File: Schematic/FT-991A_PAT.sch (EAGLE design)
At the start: 30 parts, among them Q1 PE4259, Q2 MC78L09ABDR2GOSCT, Q5 NCP553, Q7 J310, Q8 5086, X1 IF_IN, X2 SCP_OUT, X3 SDR_OUT

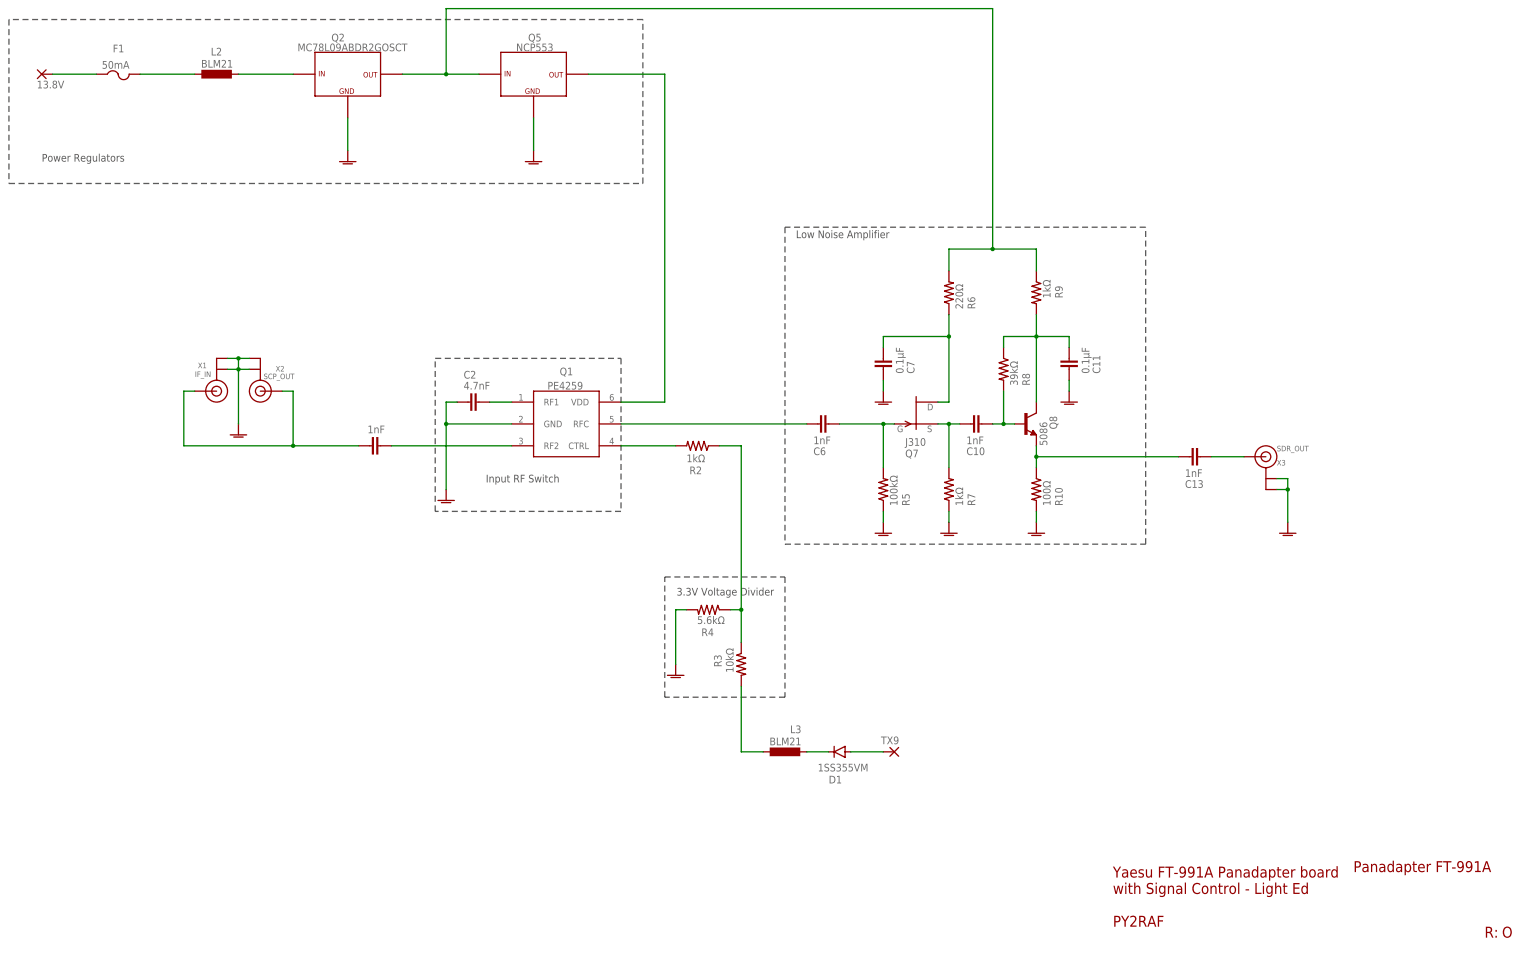
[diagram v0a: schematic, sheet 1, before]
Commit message: Starring: Revision P
* Repositioned the SDR Out port to right above the DC block cap
* Changed RF switch layout - now IF input uses the RF switch's `RFC`
  port instead of RF2 - It seems that the PE4259's `RF{N}` port gets in
  a grounded state instead of just reflecting out the data when not
  selected / active
* Got rid of the "Grounding" in RF1 port; that's not necessary
  because... Above
* Few text corrections
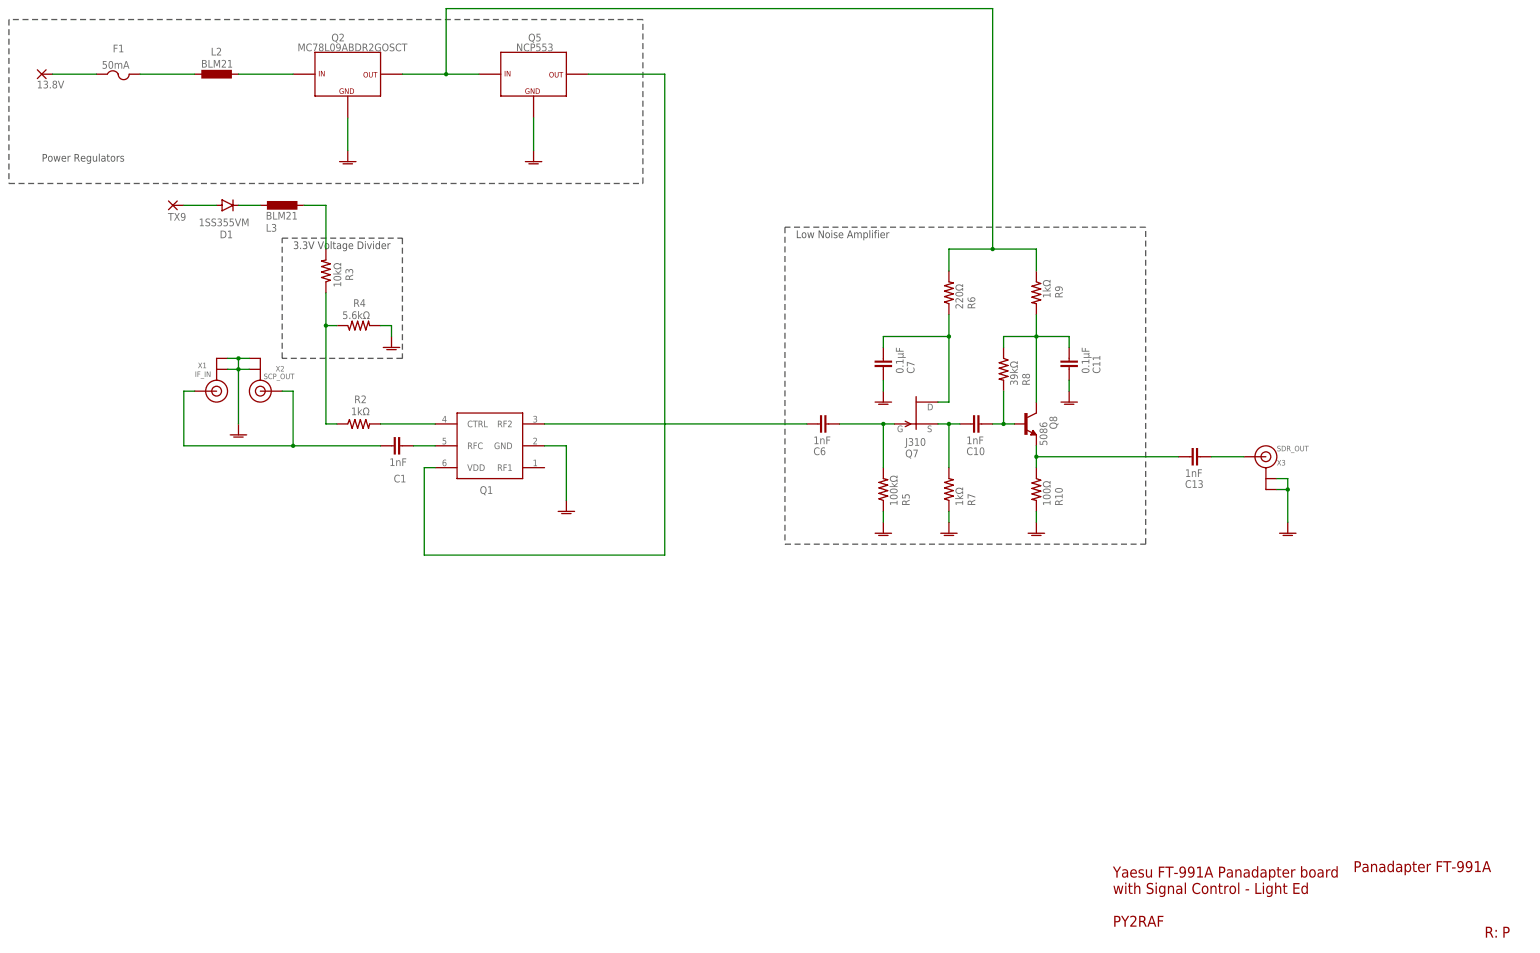
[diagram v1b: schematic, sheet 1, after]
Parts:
- removed C2: 4.7nF, rcl:C-EUC3216
- Q1: value PE4259 -> (none)
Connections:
- removed net N$21: C2.2, Q1.RF1
- removed net N$24: C1.2, Q1.RF2
- new net N$2: C1.2, Q1.RFC
- net GNDA: no longer C2.1
- net N$3: now also Q1.RF2; no longer Q1.RFC
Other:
- note removed: "DISABLE"
- note removed: "Input RF Switch"
- moved on the sheet: D1, L3, Q1, R2, R3, R4

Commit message: Board: Added test pads
Added test pads for 9V, 3V and RF Switch.
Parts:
- added TP1: 9V, testpad:TPB1,27
- added TP2, TP3: 3V, testpad:TPB1,27
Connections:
- net N$7: now also TP3.TP
- net VCC: now also TP1.TP
- net VDD: now also TP2.TP
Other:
- moved on the sheet: C1, C10, C11, C13, C6, C7, D1, F1, L2, L3, Q1, Q2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

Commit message: Preparing: Revision Q
* Better Silk-Screen Pin 1 markings for Power regulators
* Larger footprint for 2SC5086
* Moving 0.1µF transistor caps away from RF section
* Lots of re-routing
* Changing 1 nF caps to Low ESL type and 0805 footprint for better RF
  performance
* Labeled a few signals in Eagle file for better understanding of signal
  route/path
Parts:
- C1, C10, C13, C6: value 1nF -> 1000pF; device rcl:C-EUC3216 -> rcl:C-EUC0805
- Q1: value (none) -> PE4259
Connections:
- net N$10 renamed 9V5086
- net N$2 renamed IFTAP
- net N$3 renamed IFIN
- net N$37 renamed FINAL
- net N$9 renamed 9VJ310
- net VCC renamed 9V
- net VDD renamed 3V
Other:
- moved on the sheet: C13
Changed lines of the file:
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@@
 </classes>
 <parts>
-<part name="C6" library="rcl" library_urn="urn:adsk.eagle:library:334" deviceset="C-EU" device="C3216" package3d_urn="urn:adsk.eagle:package:23628/2" value="1nF"/>
+<part name="C6" library="rcl" library_urn="urn:adsk.eagle:library:334" deviceset="C-EU" device="C0805" package3d_urn="urn:adsk.eagle:package:23617/2" value="1000pF"/>
 <part name="R5" library="rcl" library_urn="urn:adsk.eagle:library:334" deviceset="R-US_" device="R3216" package3d_urn="urn:adsk.eagle:package:23557/2" value="100kΩ"/>
 <part name="Q7" library="transistor-fet" library_urn="urn:adsk.eagle:library:396" deviceset="?20*" device="SST" package3d_urn="urn:adsk.eagle:package:28534/2" technology="1" value="J310">
@@
 <part name="Q8" library="aarf" deviceset="2SC5086" device="" value="5086"/>
 <part name="R7" library="rcl" library_urn="urn:adsk.eagle:library:334" deviceset="R-US_" device="R3216" package3d_urn="urn:adsk.eagle:package:23557/2" value="1kΩ"/>
-<part name="C10" library="rcl" library_urn="urn:adsk.eagle:library:334" deviceset="C-EU" device="C3216" package3d_urn="urn:adsk.eagle:package:23628/2" value="1nF"/>
+<part name="C10" library="rcl" library_urn="urn:adsk.eagle:library:334" deviceset="C-EU" device="C0805" package3d_urn="urn:adsk.eagle:package:23617/2" value="1000pF"/>
 <part name="GND11" library="supply1" deviceset="GNDA" device=""/>
 <part name="R6" library="rcl" library_urn="urn:adsk.eagle:library:334" deviceset="R-US_" device="R3216" package3d_urn="urn:adsk.eagle:package:23557/2" value="220Ω"/>
@@
 <part name="PAD3" library="wirepad" library_urn="urn:adsk.eagle:library:412" deviceset="WIREPAD" device="SMD1,27-254" package3d_urn="urn:adsk.eagle:package:30839/1" value="TX9"/>
 <part name="R2" library="rcl" library_urn="urn:adsk.eagle:library:334" deviceset="R-US_" device="R3216" package3d_urn="urn:adsk.eagle:package:23557/2" value="1kΩ"/>
-<part name="C1" library="rcl" library_urn="urn:adsk.eagle:library:334" deviceset="C-EU" device="C3216" package3d_urn="urn:adsk.eagle:package:23628/2" value="1nF"/>
+<part name="C1" library="rcl" library_urn="urn:adsk.eagle:library:334" deviceset="C-EU" device="C0805" package3d_urn="urn:adsk.eagle:package:23617/2" value="1000pF"/>
 <part name="13.8V" library="wirepad" library_urn="urn:adsk.eagle:library:412" deviceset="WIREPAD" device="SMD1,27-254" package3d_urn="urn:adsk.eagle:package:30839/1" value="13.8V"/>
 <part name="L2" library="rcl-modified" deviceset="L-EU" device="" value="BLM21"/>
@@
 <part name="GND2" library="supply1" library_urn="urn:adsk.eagle:library:371" deviceset="GNDA" device=""/>
 <part name="L3" library="rcl-modified" deviceset="L-EU" device="" value="BLM21"/>
-<part name="C13" library="rcl" library_urn="urn:adsk.eagle:library:334" deviceset="C-EU" device="C3216" package3d_urn="urn:adsk.eagle:package:23628/2" value="1nF"/>
+<part name="C13" library="rcl" library_urn="urn:adsk.eagle:library:334" deviceset="C-EU" device="C0805" package3d_urn="urn:adsk.eagle:package:23617/2" value="1000pF"/>
 <part name="FRAME2" library="frames" library_urn="urn:adsk.eagle:library:229" deviceset="A3L-LOC" device=""/>
 <part name="GND5" library="supply1" library_urn="urn:adsk.eagle:library:371" deviceset="GNDA" device=""/>
@@
 <part name="F1" library="adafruit" deviceset="PTCFUSE" device="-1206" value="50mA"/>
 <part name="Q2" library="aarf" deviceset="MC78L" device="" technology="09ABDR2GOSCT"/>
-<part name="Q1" library="aarf" deviceset="PE4259" device=""/>
+<part name="Q1" library="aarf" deviceset="PE4259" device="" value="PE4259"/>
 <part name="GND1" library="supply1" library_urn="urn:adsk.eagle:library:371" deviceset="GNDA" device=""/>
 <part name="TP1" library="testpad" library_urn="urn:adsk.eagle:library:385" deviceset="TP" device="B1,27" package3d_urn="urn:adsk.eagle:package:27944/1" value="9V"/>
@@
 <wire x1="307.34" y1="147.32" x2="223.52" y2="147.32" width="0.1524" layer="97" style="shortdash"/>
 <text x="226.06" y="144.78" size="1.778" layer="97">Low Noise Amplifier</text>
-<text x="50.8" y="162.56" size="1.778" layer="97">Power Regulators</text>
+<text x="66.04" y="167.64" size="1.778" layer="97">Power Regulators</text>
 <text x="379.984" y="5.08" size="2.54" layer="94">&gt;REVISION_ID</text>
 </plain>
@@
 <instance part="Q8" gate="G$1" x="279.4" y="101.6" smashed="yes">
 <attribute name="NAME" x="286.766" y="100.33" size="1.778" layer="95" rot="R90"/>
-<attribute name="VALUE" x="284.48" y="96.52" size="1.778" layer="96" rot="R90"/>
+<attribute name="VALUE" x="284.48" y="99.06" size="1.778" layer="96" rot="R90"/>
 </instance>
 <instance part="R7" gate="G$1" x="261.62" y="86.36" smashed="yes" rot="R90">
@@
 <attribute name="VALUE" x="102.87" y="149.098" size="1.778" layer="96"/>
 </instance>
-<instance part="C13" gate="G$1" x="317.5" y="93.98" smashed="yes" rot="R90">
-<attribute name="NAME" x="316.484" y="86.741" size="1.778" layer="95"/>
-<attribute name="VALUE" x="316.484" y="89.281" size="1.778" layer="96"/>
+<instance part="C13" gate="G$1" x="299.72" y="93.98" smashed="yes" rot="R90">
+<attribute name="NAME" x="298.704" y="86.741" size="1.778" layer="95"/>
+<attribute name="VALUE" x="298.704" y="89.281" size="1.778" layer="96"/>
 </instance>
 <instance part="GND5" gate="1" x="165.1" y="162.56" smashed="yes"/>
@@
 </instance>
 <instance part="Q1" gate="G$1" x="154.94" y="96.52" smashed="yes" rot="R180">
-<attribute name="NAME" x="155.702" y="87.122" size="1.778" layer="95" rot="R180"/>
-<attribute name="VALUE" x="157.48" y="86.36" size="1.778" layer="96" rot="R180"/>
+<attribute name="NAME" x="157.48" y="83.82" size="1.778" layer="95" rot="R180"/>
+<attribute name="VALUE" x="159.258" y="87.63" size="1.778" layer="96" rot="R180"/>
 </instance>
 <instance part="GND1" gate="1" x="172.72" y="81.28" smashed="yes" rot="MR0"/>
@@
 <pinref part="C13" gate="G$1" pin="1"/>
 <wire x1="281.94" y1="93.98" x2="281.94" y2="91.44" width="0.1524" layer="91"/>
-<wire x1="314.96" y1="93.98" x2="281.94" y2="93.98" width="0.1524" layer="91"/>
+<wire x1="297.18" y1="93.98" x2="281.94" y2="93.98" width="0.1524" layer="91"/>
 <junction x="281.94" y="93.98"/>
 </segment>
@@
 </segment>
 </net>
-<net name="N$9" class="0">
+<net name="9VJ310" class="0">
 <segment>
 <pinref part="R6" gate="G$1" pin="1"/>
@@
 </segment>
 </net>
-<net name="N$10" class="0">
+<net name="9V5086" class="0">
 <segment>
 <pinref part="R8" gate="G$1" pin="1"/>
@@
 </segment>
 </net>
-<net name="VCC" class="0">
+<net name="9V" class="0">
 <segment>
 <pinref part="R9" gate="G$1" pin="1"/>
@@
 </segment>
 </net>
-<net name="VDD" class="0">
+<net name="3V" class="0">
 <segment>
 <wire x1="195.58" y1="71.12" x2="195.58" y2="170.18" width="0.1524" layer="91"/>
@@
 </segment>
 </net>
-<net name="N$37" class="0">
+<net name="FINAL" class="0">
 <segment>
 <pinref part="C13" gate="G$1" pin="2"/>
 <pinref part="X3" gate="G$1" pin="SIGNAL"/>
-<wire x1="322.58" y1="93.98" x2="330.2" y2="93.98" width="0.1524" layer="91"/>
+<wire x1="304.8" y1="93.98" x2="330.2" y2="93.98" width="0.1524" layer="91"/>
 </segment>
 </net>
@@
 </segment>
 </net>
-<net name="N$2" class="0">
+<net name="IFTAP" class="0">
 <segment>
 <pinref part="C1" gate="G$1" pin="2"/>
@@
 </segment>
 </net>
-<net name="N$3" class="0">
+<net name="IFIN" class="0">
 <segment>
 <pinref part="Q1" gate="G$1" pin="RF2"/>

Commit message: Minor routing hacks
- Replaced J310 JFET
  * Taking full advantage of its Source and Drain interchangeability
  * Avoiding some signal track xing
- And more routing changes.
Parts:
- Q7: device transistor-fet:SST201 -> aarf:JFET-N-SOT23-3; SPICEPREFIX J -> (none)
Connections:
- net N$27 renamed RAWIN
- net 9VJ310: now also Q7.S; no longer Q7.D
- net N$5: now also Q7.D; no longer Q7.S
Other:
- moved on the sheet: C10, C11, C13, Q8, R10, R5, R7, R8, X3

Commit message: Rev. Q more enhancements
- Changed two resistors in Amplifier chain in order to get some more
  gain - See Issue 14
- Updated BOM in order to reflect this change
- Added a ground pad, that's useful when troubleshooting and the lack
  of it bit my butt a number of times
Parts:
- added GND: GND, wirepad:WIREPADSMD1,27-254
- R10: value 100Ω -> 220Ω
- R8: value 39kΩ -> 10kΩ
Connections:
- net GNDA: now also GND.P
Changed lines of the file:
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@@
 <part name="GND10" library="supply1" deviceset="GNDA" device=""/>
 <part name="C11" library="rcl" library_urn="urn:adsk.eagle:library:334" deviceset="C-EU" device="C3216" package3d_urn="urn:adsk.eagle:package:23628/2" value="0.1µF"/>
-<part name="R8" library="rcl" library_urn="urn:adsk.eagle:library:334" deviceset="R-US_" device="R3216" package3d_urn="urn:adsk.eagle:package:23557/2" value="39kΩ"/>
+<part name="R8" library="rcl" library_urn="urn:adsk.eagle:library:334" deviceset="R-US_" device="R3216" package3d_urn="urn:adsk.eagle:package:23557/2" value="10kΩ"/>
 <part name="GND19" library="supply1" deviceset="GNDA" device=""/>
 <part name="GND13" library="supply1" deviceset="GNDA" device=""/>
 <part name="R9" library="rcl" library_urn="urn:adsk.eagle:library:334" deviceset="R-US_" device="R3216" package3d_urn="urn:adsk.eagle:package:23557/2" value="1kΩ"/>
-<part name="R10" library="rcl" library_urn="urn:adsk.eagle:library:334" deviceset="R-US_" device="R3216" package3d_urn="urn:adsk.eagle:package:23557/2" value="100Ω"/>
+<part name="R10" library="rcl" library_urn="urn:adsk.eagle:library:334" deviceset="R-US_" device="R3216" package3d_urn="urn:adsk.eagle:package:23557/2" value="220Ω"/>
 <part name="GND16" library="supply1" deviceset="GNDA" device=""/>
 <part name="X3" library="adafruit" deviceset="ANTENNA_U.FL" device="" value="SDR_OUT"/>
@@
 <part name="TP3" library="testpad" library_urn="urn:adsk.eagle:library:385" deviceset="TP" device="B1,27" package3d_urn="urn:adsk.eagle:package:27944/1" value="3V"/>
 <part name="Q7" library="aarf" deviceset="JFET-N-SOT23-3" device="" value="J310"/>
+<part name="GND" library="wirepad" library_urn="urn:adsk.eagle:library:412" deviceset="WIREPAD" device="SMD1,27-254" package3d_urn="urn:adsk.eagle:package:30839/1" value="GND"/>
+<part name="GND3" library="supply1" library_urn="urn:adsk.eagle:library:371" deviceset="GNDA" device=""/>
 </parts>
 <sheets>
@@
 <attribute name="VALUE" x="254" y="99.06" size="1.778" layer="96" rot="MR180"/>
 </instance>
+<instance part="GND" gate="G$1" x="50.8" y="170.18" smashed="yes">
+<attribute name="VALUE" x="49.657" y="166.878" size="1.778" layer="96"/>
+</instance>
+<instance part="GND3" gate="1" x="58.42" y="160.02" smashed="yes"/>
 </instances>
 <busses>
@@
 <wire x1="172.72" y1="96.52" x2="172.72" y2="83.82" width="0.1524" layer="91"/>
 </segment>
-</net>
+<segment>
+<pinref part="GND" gate="G$1" pin="P"/>
+<pinref part="GND3" gate="1" pin="GNDA"/>
+<wire x1="53.34" y1="170.18" x2="58.42" y2="170.18" width="0.1524" layer="91"/>
+<wire x1="58.42" y1="170.18" x2="58.42" y2="162.56" width="0.1524" layer="91"/>
+</segment>
+</net>
